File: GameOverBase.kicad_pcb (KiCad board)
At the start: 4 copper layers, 50 x 35 mm, 49 parts, among them J1 USB_C_DEALON-USB-US31-106, J2 Serial Port, J3 add-on conn, Q1 PMN48XP, SW1 SW_DIP_x08, SW2 boot, SW3 Reset, U1 ESP32-WROOM-E, U2 4021, U3 MCP73831-2ACI-OT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

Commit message: Puts screw holes on the PCB
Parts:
- moved H2 102.5 mm to (123.0, 112.0)
- moved H1 65.3 mm to (167.0, 83.0)
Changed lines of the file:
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@@
     )
   )
-  (footprint "MountingHole:MountingHole_2.2mm_M2_Pad_Via" (layer "F.Cu")
-    (at 229.71 64.8)
+  (footprint "MountingHole:MountingHole_2.2mm_M2_Pad_Via" locked (layer "F.Cu")
+    (at 167 83)
     (descr "Mounting Hole 2.2mm, M2")
     (tags "mounting hole 2.2mm m2")
@@
     (property "Sheetname" "")
     (attr exclude_from_pos_files)
-    (fp_text reference "H1" (at 0 -3.2) (layer "F.SilkS")
+    (fp_text reference "H1" (at 0 -3.2) (layer "F.SilkS") hide
         (effects (font (size 1 1) (thickness 0.15)))
     )
@@
     (fp_circle (center 0 0) (end 2.45 0)
       (stroke (width 0.05) (type solid)) (fill none) (layer "F.CrtYd"))
-    (pad "1" thru_hole circle (at -1.65 0) (size 0.7 0.7) (drill 0.4) (layers *.Cu *.Mask)
-      (net 2 "GND") (pinfunction "1") (pintype "input"))
-    (pad "1" thru_hole circle (at -1.166726 -1.166726) (size 0.7 0.7) (drill 0.4) (layers *.Cu *.Mask)
-      (net 2 "GND") (pinfunction "1") (pintype "input"))
-    (pad "1" thru_hole circle (at -1.166726 1.166726) (size 0.7 0.7) (drill 0.4) (layers *.Cu *.Mask)
-      (net 2 "GND") (pinfunction "1") (pintype "input"))
-    (pad "1" thru_hole circle (at 0 -1.65) (size 0.7 0.7) (drill 0.4) (layers *.Cu *.Mask)
-      (net 2 "GND") (pinfunction "1") (pintype "input"))
-    (pad "1" thru_hole circle (at 0 0) (size 4.4 4.4) (drill 2.2) (layers *.Cu *.Mask)
-      (net 2 "GND") (pinfunction "1") (pintype "input"))
-    (pad "1" thru_hole circle (at 0 1.65) (size 0.7 0.7) (drill 0.4) (layers *.Cu *.Mask)
-      (net 2 "GND") (pinfunction "1") (pintype "input"))
-    (pad "1" thru_hole circle (at 1.166726 -1.166726) (size 0.7 0.7) (drill 0.4) (layers *.Cu *.Mask)
-      (net 2 "GND") (pinfunction "1") (pintype "input"))
-    (pad "1" thru_hole circle (at 1.166726 1.166726) (size 0.7 0.7) (drill 0.4) (layers *.Cu *.Mask)
-      (net 2 "GND") (pinfunction "1") (pintype "input"))
-    (pad "1" thru_hole circle (at 1.65 0) (size 0.7 0.7) (drill 0.4) (layers *.Cu *.Mask)
+    (pad "1" thru_hole circle locked (at -1.65 0) (size 0.7 0.7) (drill 0.4) (layers *.Cu *.Mask)
+      (net 2 "GND") (pinfunction "1") (pintype "input"))
+    (pad "1" thru_hole circle locked (at -1.166726 -1.166726) (size 0.7 0.7) (drill 0.4) (layers *.Cu *.Mask)
+      (net 2 "GND") (pinfunction "1") (pintype "input"))
+    (pad "1" thru_hole circle locked (at -1.166726 1.166726) (size 0.7 0.7) (drill 0.4) (layers *.Cu *.Mask)
+      (net 2 "GND") (pinfunction "1") (pintype "input"))
+    (pad "1" thru_hole circle locked (at 0 -1.65) (size 0.7 0.7) (drill 0.4) (layers *.Cu *.Mask)
+      (net 2 "GND") (pinfunction "1") (pintype "input"))
+    (pad "1" thru_hole circle locked (at 0 0) (size 4.4 4.4) (drill 2.2) (layers *.Cu *.Mask)
+      (net 2 "GND") (pinfunction "1") (pintype "input"))
+    (pad "1" thru_hole circle locked (at 0 1.65) (size 0.7 0.7) (drill 0.4) (layers *.Cu *.Mask)
+      (net 2 "GND") (pinfunction "1") (pintype "input"))
+    (pad "1" thru_hole circle locked (at 1.166726 -1.166726) (size 0.7 0.7) (drill 0.4) (layers *.Cu *.Mask)
+      (net 2 "GND") (pinfunction "1") (pintype "input"))
+    (pad "1" thru_hole circle locked (at 1.166726 1.166726) (size 0.7 0.7) (drill 0.4) (layers *.Cu *.Mask)
+      (net 2 "GND") (pinfunction "1") (pintype "input"))
+    (pad "1" thru_hole circle locked (at 1.65 0) (size 0.7 0.7) (drill 0.4) (layers *.Cu *.Mask)
       (net 2 "GND") (pinfunction "1") (pintype "input"))
   )
@@
       (thermal_bridge_angle 45))
   )
-  (footprint "MountingHole:MountingHole_2.2mm_M2_Pad_Via" (layer "F.Cu")
-    (at 218.36 74.35)
+  (footprint "MountingHole:MountingHole_2.2mm_M2_Pad_Via" locked (layer "F.Cu")
+    (at 123 112)
     (descr "Mounting Hole 2.2mm, M2")
     (tags "mounting hole 2.2mm m2")
@@
     (property "Sheetname" "")
     (attr exclude_from_pos_files)
-    (fp_text reference "H2" (at 0 -3.2) (layer "F.SilkS")
+    (fp_text reference "H2" (at 0 -3.2) (layer "F.SilkS") hide
         (effects (font (size 1 1) (thickness 0.15)))
     )
@@
     (fp_circle (center 0 0) (end 2.45 0)
       (stroke (width 0.05) (type solid)) (fill none) (layer "F.CrtYd"))
-    (pad "1" thru_hole circle (at -1.65 0) (size 0.7 0.7) (drill 0.4) (layers *.Cu *.Mask)
-      (net 2 "GND") (pinfunction "1") (pintype "input"))
-    (pad "1" thru_hole circle (at -1.166726 -1.166726) (size 0.7 0.7) (drill 0.4) (layers *.Cu *.Mask)
-      (net 2 "GND") (pinfunction "1") (pintype "input"))
-    (pad "1" thru_hole circle (at -1.166726 1.166726) (size 0.7 0.7) (drill 0.4) (layers *.Cu *.Mask)
-      (net 2 "GND") (pinfunction "1") (pintype "input"))
-    (pad "1" thru_hole circle (at 0 -1.65) (size 0.7 0.7) (drill 0.4) (layers *.Cu *.Mask)
-      (net 2 "GND") (pinfunction "1") (pintype "input"))
-    (pad "1" thru_hole circle (at 0 0) (size 4.4 4.4) (drill 2.2) (layers *.Cu *.Mask)
-      (net 2 "GND") (pinfunction "1") (pintype "input"))
-    (pad "1" thru_hole circle (at 0 1.65) (size 0.7 0.7) (drill 0.4) (layers *.Cu *.Mask)
-      (net 2 "GND") (pinfunction "1") (pintype "input"))
-    (pad "1" thru_hole circle (at 1.166726 -1.166726) (size 0.7 0.7) (drill 0.4) (layers *.Cu *.Mask)
-      (net 2 "GND") (pinfunction "1") (pintype "input"))
-    (pad "1" thru_hole circle (at 1.166726 1.166726) (size 0.7 0.7) (drill 0.4) (layers *.Cu *.Mask)
-      (net 2 "GND") (pinfunction "1") (pintype "input"))
-    (pad "1" thru_hole circle (at 1.65 0) (size 0.7 0.7) (drill 0.4) (layers *.Cu *.Mask)
-      (net 2 "GND") (pinfunction "1") (pintype "input"))
-  )
+    (pad "1" thru_hole circle locked (at -1.65 0) (size 0.7 0.7) (drill 0.4) (layers *.Cu *.Mask)
+      (net 2 "GND") (pinfunction "1") (pintype "input"))
+    (pad "1" thru_hole circle locked (at -1.166726 -1.166726) (size 0.7 0.7) (drill 0.4) (layers *.Cu *.Mask)
+      (net 2 "GND") (pinfunction "1") (pintype "input"))
+    (pad "1" thru_hole circle locked (at -1.166726 1.166726) (size 0.7 0.7) (drill 0.4) (layers *.Cu *.Mask)
+      (net 2 "GND") (pinfunction "1") (pintype "input"))
+    (pad "1" thru_hole circle locked (at 0 -1.65) (size 0.7 0.7) (drill 0.4) (layers *.Cu *.Mask)
+      (net 2 "GND") (pinfunction "1") (pintype "input"))
+    (pad "1" thru_hole circle locked (at 0 0) (size 4.4 4.4) (drill 2.2) (layers *.Cu *.Mask)
+      (net 2 "GND") (pinfunction "1") (pintype "input"))
+    (pad "1" thru_hole circle locked (at 0 1.65) (size 0.7 0.7) (drill 0.4) (layers *.Cu *.Mask)
+      (net 2 "GND") (pinfunction "1") (pintype "input"))
+    (pad "1" thru_hole circle locked (at 1.166726 -1.166726) (size 0.7 0.7) (drill 0.4) (layers *.Cu *.Mask)
+      (net 2 "GND") (pinfunction "1") (pintype "input"))
+    (pad "1" thru_hole circle locked (at 1.166726 1.166726) (size 0.7 0.7) (drill 0.4) (layers *.Cu *.Mask)
+      (net 2 "GND") (pinfunction "1") (pintype "input"))
+    (pad "1" thru_hole circle locked (at 1.65 0) (size 0.7 0.7) (drill 0.4) (layers *.Cu *.Mask)
+      (net 2 "GND") (pinfunction "1") (pintype "input"))
+  )

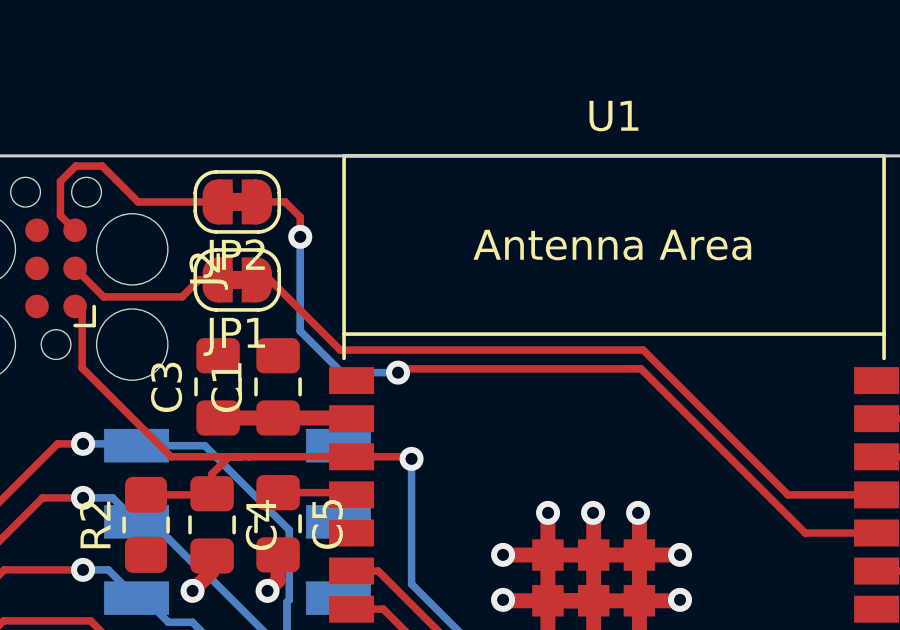
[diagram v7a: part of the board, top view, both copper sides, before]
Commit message: Adds keepout area for ESP32 antenna
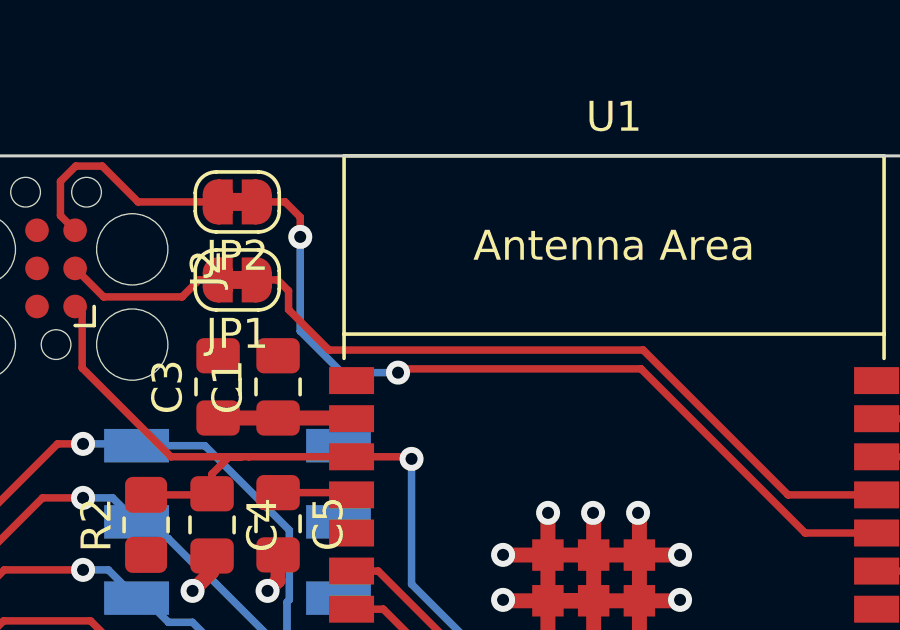
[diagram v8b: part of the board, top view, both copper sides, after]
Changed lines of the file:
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@@
   (segment (start 128.93402 107.44) (end 128.93402 113.620218) (width 0.25) (layer "B.Cu") (net 34))
   (segment (start 126.14952 105.4) (end 128.18952 107.44) (width 0.25) (layer "B.Cu") (net 34))
+  (segment (start 134 84.5) (end 134 85.125) (width 0.25) (layer "F.Cu") (net 35))
   (segment (start 150.65 91.3) (end 153.6 91.3) (width 0.25) (layer "F.Cu") (net 35))
-  (segment (start 132.94 84.135) (end 133.385 84.135) (width 0.25) (layer "F.Cu") (net 35))
   (segment (start 145.8225 86.4725) (end 150.65 91.3) (width 0.25) (layer "F.Cu") (net 35))
-  (segment (start 133.385 84.135) (end 135.7225 86.4725) (width 0.25) (layer "F.Cu") (net 35))
-  (segment (start 135.7225 86.4725) (end 145.8225 86.4725) (width 0.25) (layer "F.Cu") (net 35))
+  (segment (start 133.635 84.135) (end 132.94 84.135) (width 0.25) (layer "F.Cu") (net 35))
+  (segment (start 134 85.125) (end 135.3475 86.4725) (width 0.25) (layer "F.Cu") (net 35))
+  (segment (start 135.3475 86.4725) (end 145.8225 86.4725) (width 0.25) (layer "F.Cu") (net 35))
+  (segment (start 134 84.5) (end 133.635 84.135) (width 0.25) (layer "F.Cu") (net 35))
   (segment (start 153.6 92.57) (end 151.22 92.57) (width 0.25) (layer "F.Cu") (net 36))
   (segment (start 145.75 87.1) (end 137.7745 87.1) (width 0.25) (layer "F.Cu") (net 36))
@@
   (via (at 139.1 101.1) (size 0.8) (drill 0.4) (layers "F.Cu" "B.Cu") (net 50))
   (segment (start 139.1 101.1) (end 134.67306 101.1) (width 0.25) (layer "B.Cu") (net 50))
+  (zone (net 0) (net_name "") (layers "F.Cu" "In1.Cu" "In2.Cu" "B.Cu") (name "Antenna_keepout") (hatch edge 0.508)
+    (connect_pads (clearance 0))
+    (min_thickness 0.254) (filled_areas_thickness no)
+    (keepout (tracks not_allowed) (vias not_allowed) (pads not_allowed ) (copperpour not_allowed) (footprints allowed))
+    (fill (thermal_gap 0.508) (thermal_bridge_width 0.508) (island_removal_mode 2) (island_area_min 10))
+    (polygon
+      (pts
+        (xy 154.5 86)
+        (xy 135.3 86)
+        (xy 135.3 80)
+        (xy 154.5 80)
+      )
+    )
+  )
   (group "" (id 02ad5737-a7ad-458d-8ad3-5476d8afc17b)
     (members
